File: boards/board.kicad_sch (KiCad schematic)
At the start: 58 parts, among them J1 Conn_01x02, J2 Conn_01x02, J3 Conn_01x03, J4 Conn_01x06, J5 Conn_01x05, J6 Conn_01x02, J7 Conn_02x03_Odd_Even, J8 Conn_02x05_Odd_Even, Q1 2N2907, Q2 2n2222, Q3 IRF4905, Q4 2N7000, SW1 Switch, U1 ESP32-WROOM-32U, U2 LM393, U3 LM7805_TO220, U4 LM1117DT-ADJ, U5 LM1117DT-ADJ

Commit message: update PCB and create gerber
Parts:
- C1, C10, C2, C4, C6, C9: LCSC (none) -> C110254
- C11, C8: footprint Capacitor_THT:CP_Radial_Tantal_D5.5mm_P2.50mm -> easyeda2kicad:CAP-TH_BD5.0-P2.00-D0.8-FD; LCSC (none) -> C106654
- C12: footprint Capacitor_THT:CP_Radial_D5.0mm_P2.50mm -> easyeda2kicad:CAP-TH_BD5.0-P2.00-D0.8-FD; LCSC (none) -> C165586
- C3: footprint Capacitor_THT:CP_Radial_Tantal_D6.0mm_P2.50mm -> easyeda2kicad:CAP-TH_BD4.0-P1.50-D0.8-FD; LCSC (none) -> C43845
- C5: LCSC (none) -> C125389
- C7: footprint Capacitor_THT:CP_Radial_Tantal_D5.5mm_P2.50mm -> easyeda2kicad:CAP-TH_BD5.0-P2.00-D0.8-FD; LCSC (none) -> C165586
- D1: LCSC (none) -> C261229
- D2: LCSC (none) -> C9211
- D3: footprint Diode_THT:D_DO-41_SOD81_P10.16mm_Horizontal -> easyeda2kicad:DO-41_BD2.4-L4.7-P8.70-D0.9-RD; LCSC (none) -> C5359862
- F1, J1, J2, J6, SW1: LCSC (none) -> C239362
- J3: LCSC (none) -> C239363
- J4: LCSC (none) -> C239366
- J5: LCSC (none) -> C239365
- J7: LCSC (none) -> C11214
- J8: LCSC (none) -> C5665
- Q1: footprint Package_TO_SOT_THT:TO-92_Inline -> easyeda2kicad:TO-92-3_L4.8-W3.7-P2.54-R; LCSC (none) -> C358534
- Q2: LCSC (none) -> C118536
- Q3: LCSC (none) -> C2564
- Q4: LCSC (none) -> C9114
- R1, R2, R5, R7: footprint Resistor_THT:R_Axial_DIN0207_L6.3mm_D2.5mm_P7.62mm_Horizontal -> easyeda2kicad:RES-TH_BD2.3-L6.5-P10.50-D0.5; LCSC (none) -> C119347
- R10: footprint Resistor_THT:R_Axial_DIN0207_L6.3mm_D2.5mm_P7.62mm_Horizontal -> easyeda2kicad:RES-TH_BD4.5-L11.0-P15.00-D0.7; LCSC (none) -> C479307
- R11: footprint Resistor_THT:R_Axial_DIN0207_L6.3mm_D2.5mm_P7.62mm_Horizontal -> easyeda2kicad:RES-TH_BD2.3-L6.5-P10.50-D0.5; LCSC (none) -> C119353
- R12: footprint Resistor_THT:R_Axial_DIN0207_L6.3mm_D2.5mm_P7.62mm_Horizontal -> easyeda2kicad:RES-TH_BD2.3-L6.5-P10.50-D0.5; LCSC (none) -> C714012
- R3, R4, R6: footprint Resistor_THT:R_Axial_DIN0207_L6.3mm_D2.5mm_P7.62mm_Horizontal -> easyeda2kicad:RES-TH_BD2.3-L6.5-P10.50-D0.5; LCSC (none) -> C119324
- R8: footprint Resistor_THT:R_Axial_DIN0207_L6.3mm_D2.5mm_P7.62mm_Horizontal -> easyeda2kicad:RES-TH_BD2.3-L6.5-P10.50-D0.5; LCSC (none) -> C385454
- R9: value 50k -> 51k; footprint Resistor_THT:R_Axial_DIN0207_L6.3mm_D2.5mm_P7.62mm_Horizontal -> easyeda2kicad:RES-TH_BD2.3-L6.5-P10.50-D0.5; LCSC (none) -> C119363
- RV1: LCSC (none) -> C780119
- RV2, RV3: LCSC (none) -> C780120
- U1: value ESP32-WROOM-32U -> ESP32-WROOM-32D; footprint RF_Module:ESP32-WROOM-32 -> RF_Module:ESP32-WROOM-32D; symbol RF_Module:ESP32-WROOM-32U -> RF_Module:ESP32-WROOM-32D; LCSC (none) -> C473012
- U2: LCSC (none) -> C725322
- U3: LCSC (none) -> C3795
- U4, U5: LCSC (none) -> C498319
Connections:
- net +3V3: no longer J8.1 (Pin_1)
- net +5V: now also J8.1 (Pin_1)
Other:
- moved on the sheet: C11, C8

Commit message: Ajust J7 component
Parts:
- J3: LCSC C239363 -> C29275
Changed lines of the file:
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@@
 			)
 		)
-		(property "LCSC" "C239363"
+		(property "LCSC" "C29275"
 			(at 118.11 167.64 0)
 			(effects

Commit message: Fiz positon components, add Fabiano seal
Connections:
- net GND: now also J3.1 (Pin_1); no longer J3.3 (Pin_3)
- net PH_K: now also J3.3 (Pin_3); no longer J3.1 (Pin_1)
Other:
- moved on the sheet: J3
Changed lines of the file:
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@@
 	(symbol
 		(lib_id "Connector_Generic:Conn_01x03")
-		(at 116.84 176.53 0)
-		(mirror y)
+		(at 116.84 176.53 180)
 		(unit 1)
 		(exclude_from_sim no)
@@
 		)
 		(property "LCSC" "C29275"
-			(at 118.11 167.64 0)
+			(at 118.11 185.42 0)
 			(effects
 				(font

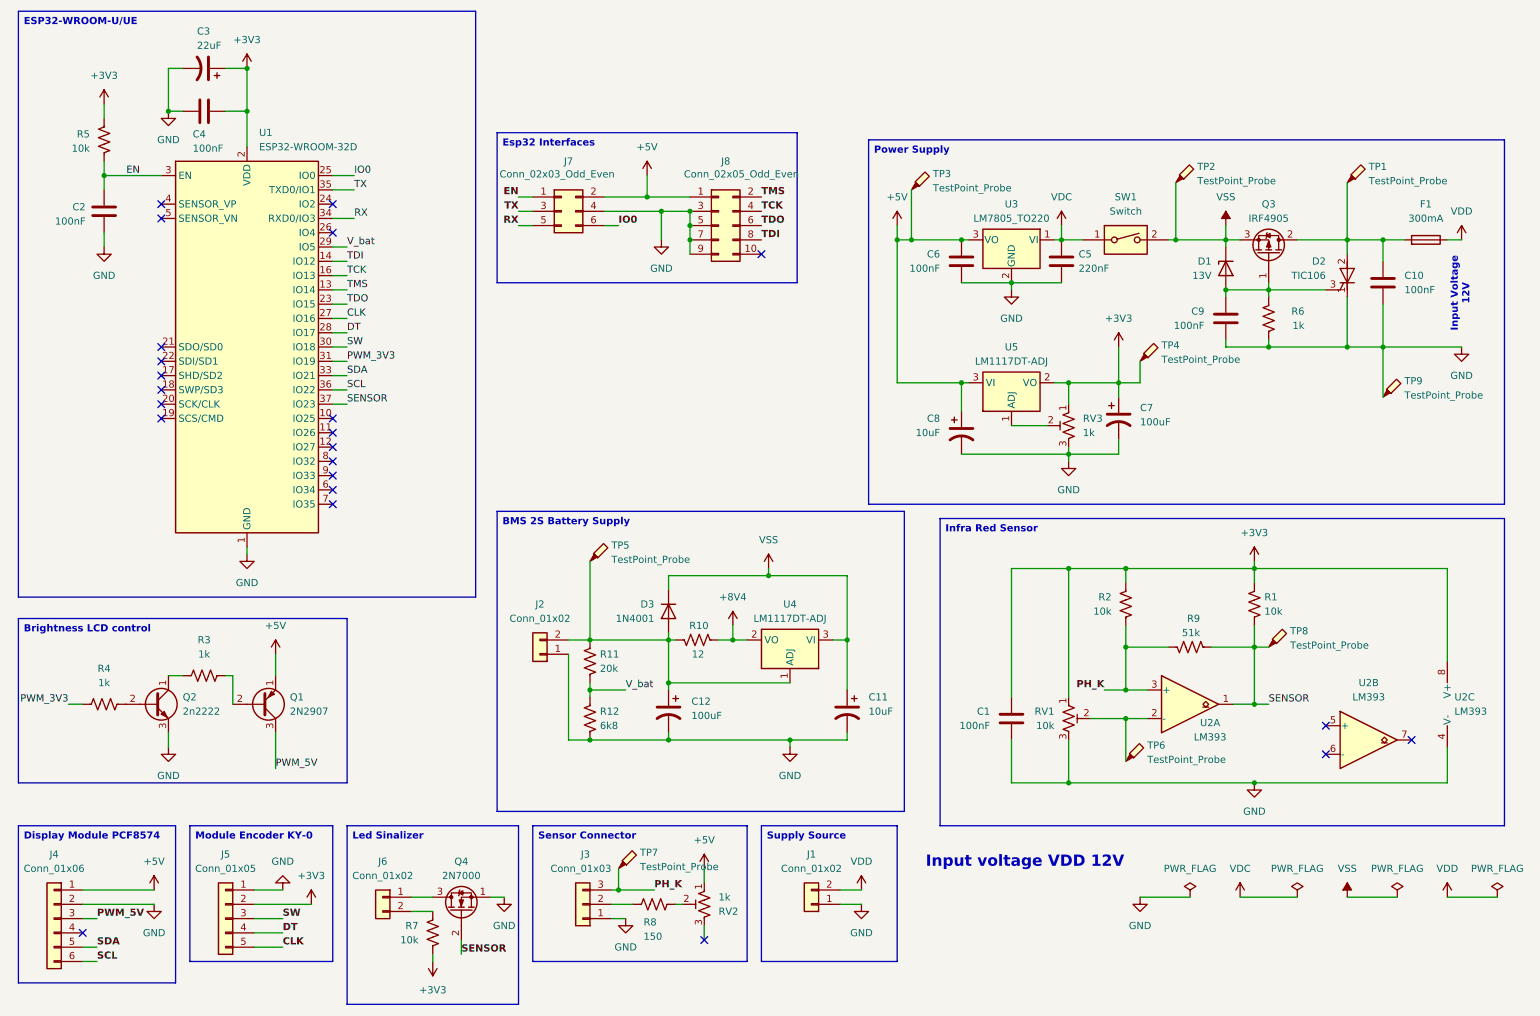
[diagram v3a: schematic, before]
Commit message: rename modules in sketch
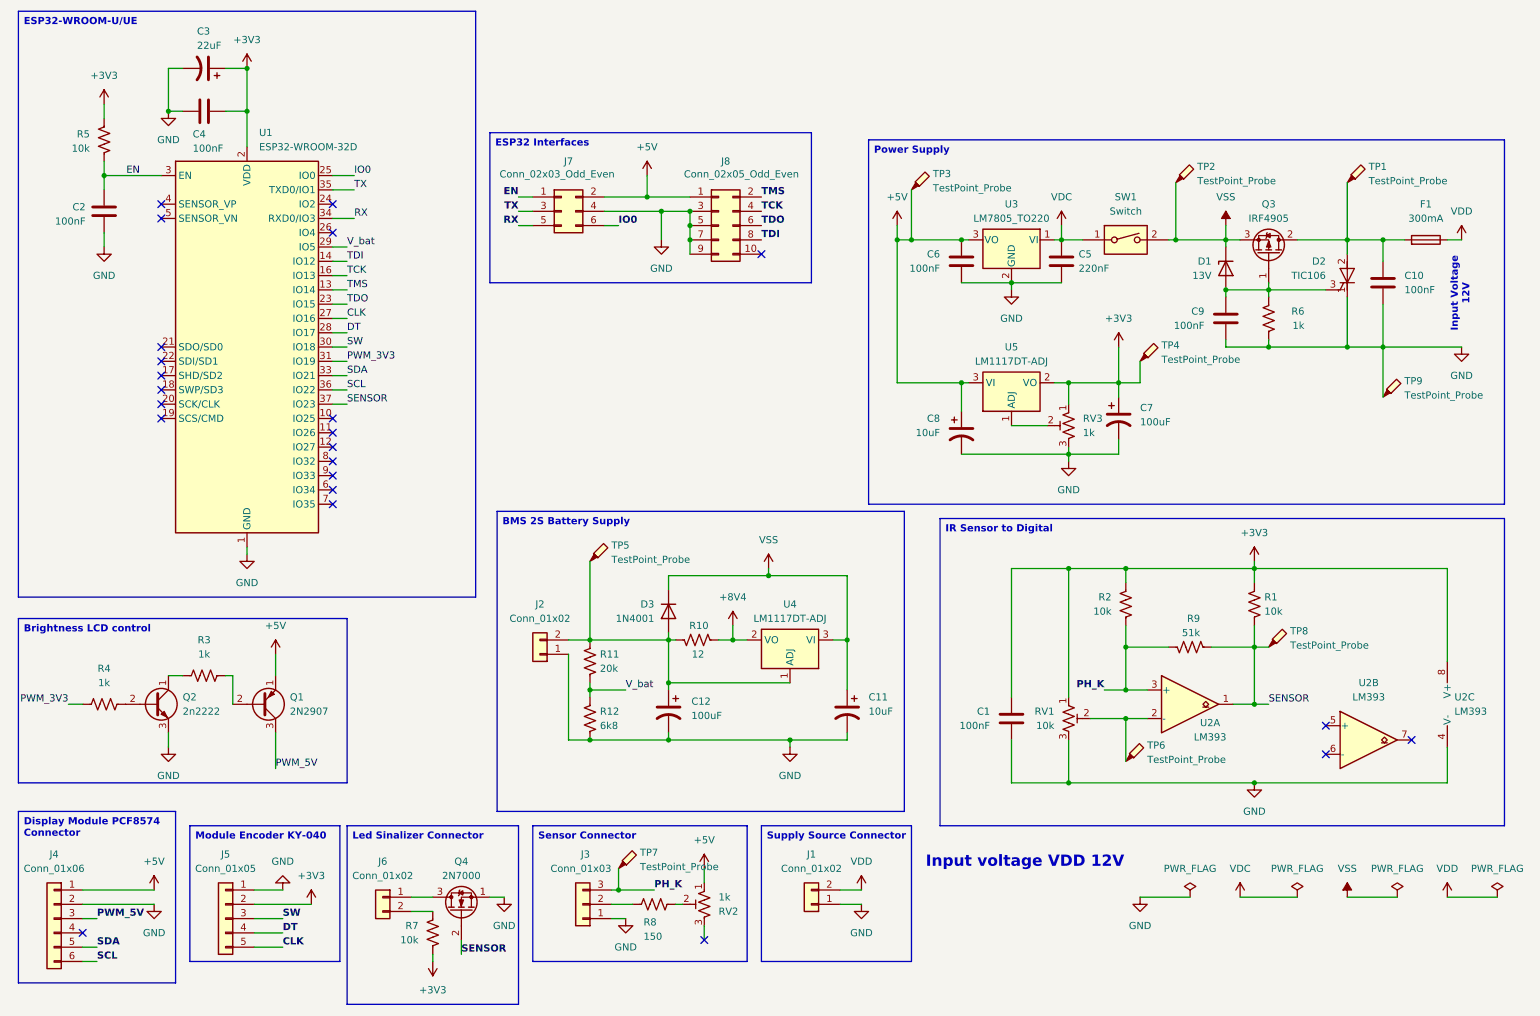
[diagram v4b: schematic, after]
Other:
- title: (none) -> Phtogate V2
